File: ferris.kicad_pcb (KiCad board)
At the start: 2 copper layers, 225 x 95.2 mm, 99 parts, among them J1 USB C, K0_0 KEYSW, K0_1 KEYSW, K0_2 KEYSW, K0_3 KEYSW, K0_4 KEYSW, K0_5 KEYSW, K0_6 KEYSW, K0_7 KEYSW, K0_8 KEYSW, K0_9 KEYSW, K1_0 KEYSW, K1_1 KEYSW, K1_2 KEYSW, K1_3 KEYSW, K1_4 KEYSW, K1_5 KEYSW, K1_6 KEYSW, K1_7 KEYSW, K1_8 KEYSW, K1_9 KEYSW, K2_0 KEYSW, K2_1 KEYSW, K2_2 KEYSW, K2_3 KEYSW, K2_4 KEYSW, K2_5 KEYSW, K2_6 KEYSW, K2_7 KEYSW, K2_8 KEYSW, K2_9 KEYSW, K3_3 KEYSW, K3_4 KEYSW, K3_5 KEYSW, K3_6 KEYSW, SW1 Reset, U1 ATmega32U4-AU, U2 MCP23017_SO, Y1 Crystal

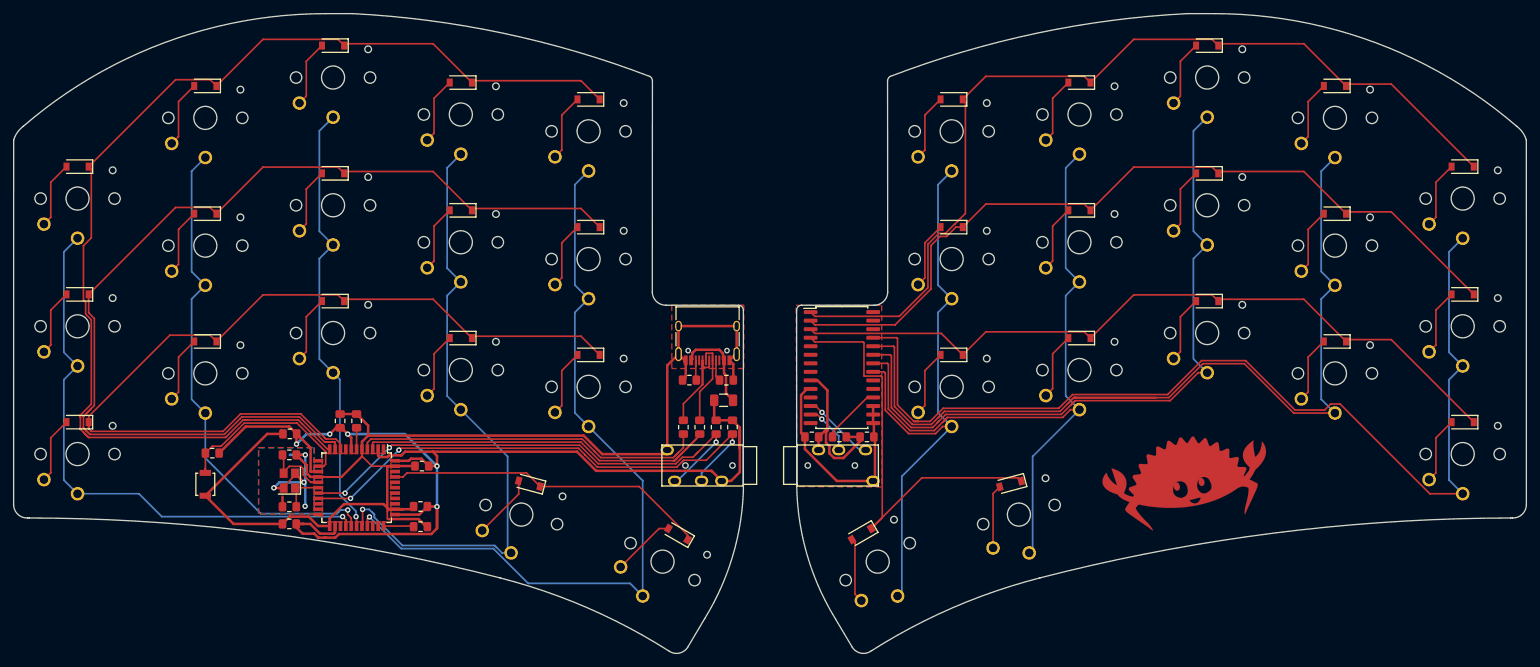
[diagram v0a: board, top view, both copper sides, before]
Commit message: Design the "Ferris low" variant
* Same as the base variant with major change that the footprints are
  for Kailh PG1232 instead of choc for an even lower profile
* Copper pad adapted to ducking Ferris for theme
* Silkscreen changed to display schematics from the PG1232 switch
* Recommended PCB solder mask color is blue instead of white so the
  silkscreen gives vibes of a blueprint
* Name of the board updated to "Ferris low" instead of "Ferris"
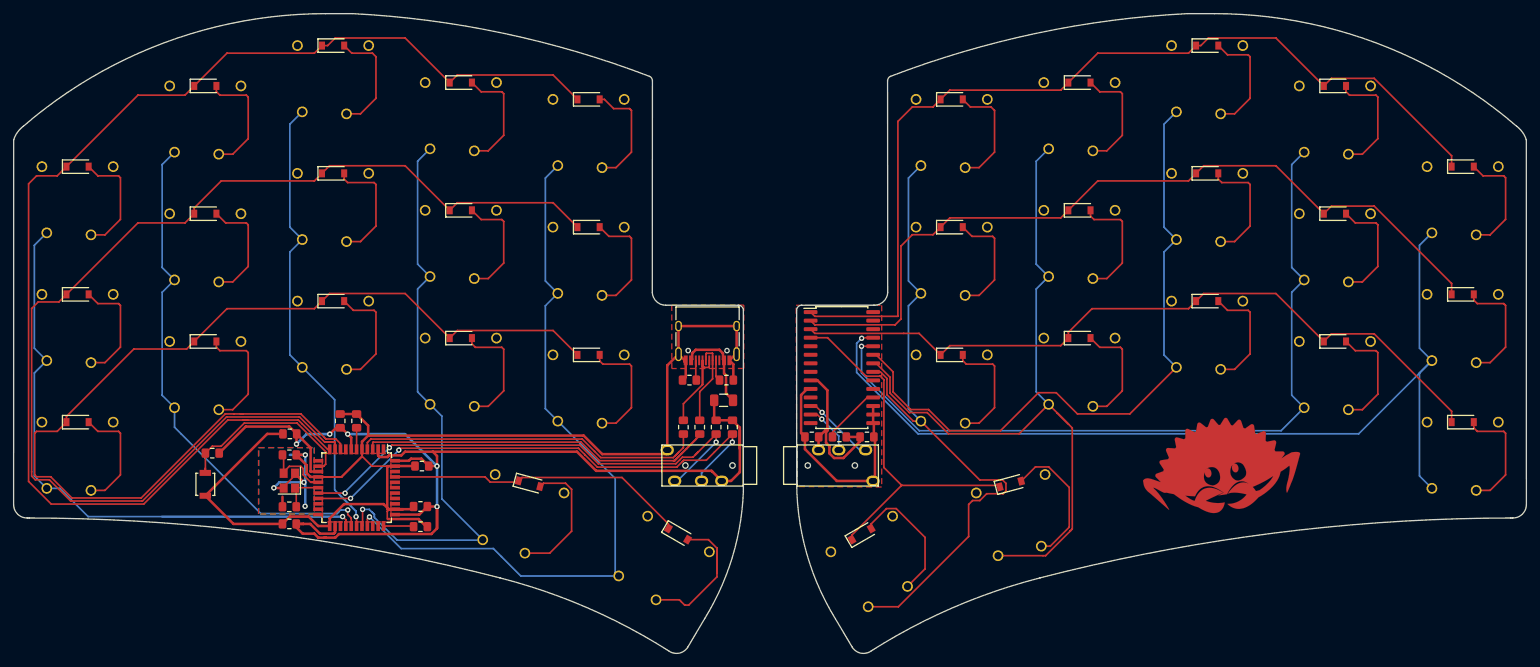
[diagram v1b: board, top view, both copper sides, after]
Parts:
- removed the G*** at (67.9, 61.3)
- removed the G*** at (186.4, 53.0)
- removed the G*** at (188.0, 83.0) (x2)
- added G***: LOGO, ferris:ducking_ferris_pad, F.Cu at (193.3, 80.3)
- added REF**: silk_pg1232_side, ferris:silk_pg1232_side, B.Cu at (27.9, 30.2)
- added REF**: silk_pg1232_schematic, ferris:silk_pg1232_schematic, B.Cu at (225.2, 29.5)
- added REF**: silk_pg1232_right, ferris:silk_pg1232_right, B.Cu at (140.8, 70.5)
- added REF**: silk_pg1232_left, ferris:silk_pg1232_left, B.Cu at (115.7, 69.8)
- added REF**: silk_pg1232_bottom, ferris:silk_pg1232_bottom, B.Cu at (182.3, 85.1)
- added REF**: silk_pg2132_top, ferris:silk_pg2132_top, B.Cu at (207.0, 80.9)
- added REF**: silk_pg1232_footprint, ferris:silk_pg1232_footprint, B.Cu at (61.3, 80.3)
- C1, C2: value 22pF -> 22p
- C10, C3, C4, C5, C6, C9: value 0.1uF -> 0.1u
- C7: value 4.7uF -> 4.7u
- C8: value 1uF -> 1u
- K0_0, K0_1, K0_2, K0_3, K0_4, K0_5, K0_6, K0_7, K0_8, K0_9, K1_0, K1_1, K1_2, K1_3, K1_4, K1_5, K1_6, K1_7, K1_8, K1_9, K2_0, K2_1, K2_2, K2_3, K2_4, K2_5, K2_6, K2_7, K2_8, K2_9, K3_3, K3_4, K3_5, K3_6: footprint ferris:SW_PG1350 -> ferris:Kailh_PG1232
- R1, R2, R9: value 10kΩ -> 10k
- R3, R4: value 22Ω -> 22
- R5, R6: value 5.1KΩ -> 5.1K
- R7, R8: value 4.7kΩ -> 4.7k
- SW1: value Reset -> SW_PUSH
- turned D0_0 to 0 degrees
- turned D0_1 to 0 degrees
- turned D0_2 to 0 degrees
- turned D0_3 to 0 degrees
- turned D0_4 to 0 degrees
- turned D0_5 to 0 degrees
- turned D0_6 to 0 degrees
- turned D0_7 to 0 degrees
- turned D0_8 to 0 degrees
- turned D0_9 to 0 degrees
- turned D1_0 to 0 degrees
- turned D1_1 to 0 degrees
- turned D1_2 to 0 degrees
- turned D1_3 to 0 degrees
- turned D1_4 to 0 degrees
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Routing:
- net /col0: track 83.8 -> 115.3 mm
- net /col8: track 141.1 -> 117.6 mm, vias 0 -> 1
- net /row0,2: track 132.5 -> 155.9 mm
- net /row0,0: track 172.0 -> 193.7 mm
- net /row0,1: track 155.6 -> 175.8 mm
- net Net-(D3_4-Pad2): track 9.47 -> 24.4 mm
- net /col5: track 89.1 -> 101.5 mm
- net /col9: track 153.3 -> 142.0 mm, vias 0 -> 1
- net Net-(D3_6-Pad2): track 9.50 -> 20.5 mm
- net Net-(D3_3-Pad2): track 9.65 -> 19.8 mm
- net Net-(D3_5-Pad2): track 9.65 -> 19.8 mm
- net /row1,3: track 65.0 -> 56.1 mm
- net Net-(D2_4-Pad2): track 9.94 -> 17.5 mm
- net Net-(D2_9-Pad2): track 9.94 -> 17.4 mm
- net Net-(D1_9-Pad2): track 9.94 -> 17.4 mm
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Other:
- board text added: "Ferris low v0.1"
- board text removed: "Ferris v0.1"
- board text removed: "Illustration adapted from "Safe and unsafe rust" by @whoisaldeka"

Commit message: Update silkscreen text to credit bomtarnes and for uppercasing Low
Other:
- board text added: "Ferris Low v0.1"
- board text added: "by @pierrec83 and bomtarnes"
- board text removed: "Ferris low v0.1"
- board text removed: "by @pierrec83"
